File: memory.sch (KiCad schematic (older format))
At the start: 6 parts

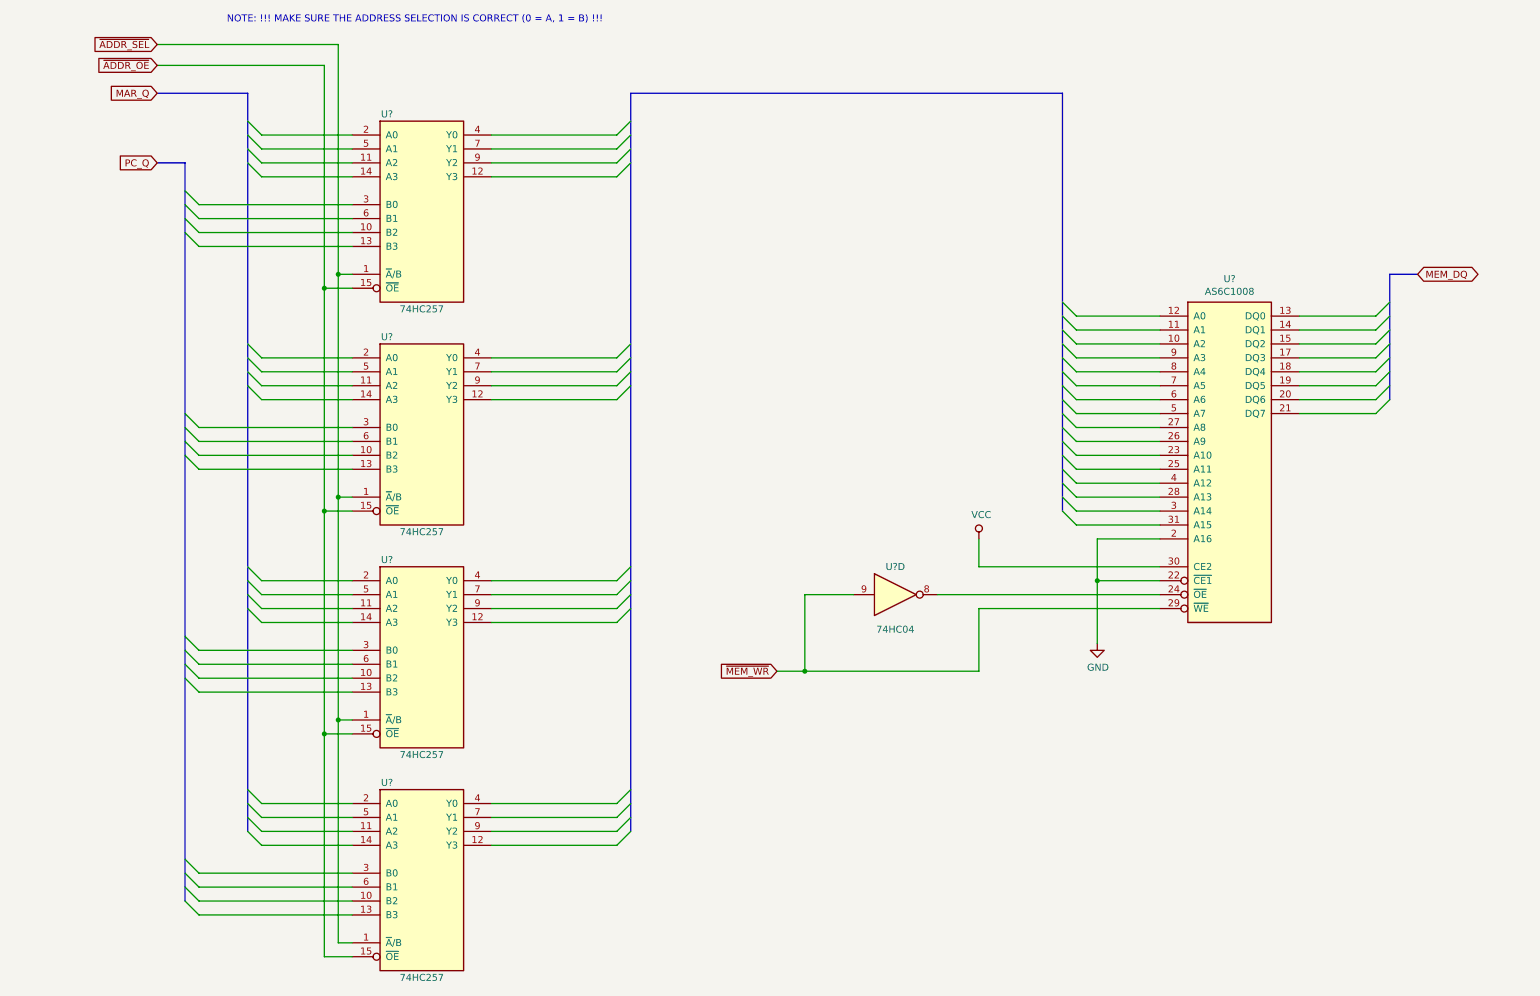
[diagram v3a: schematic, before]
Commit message: added labels
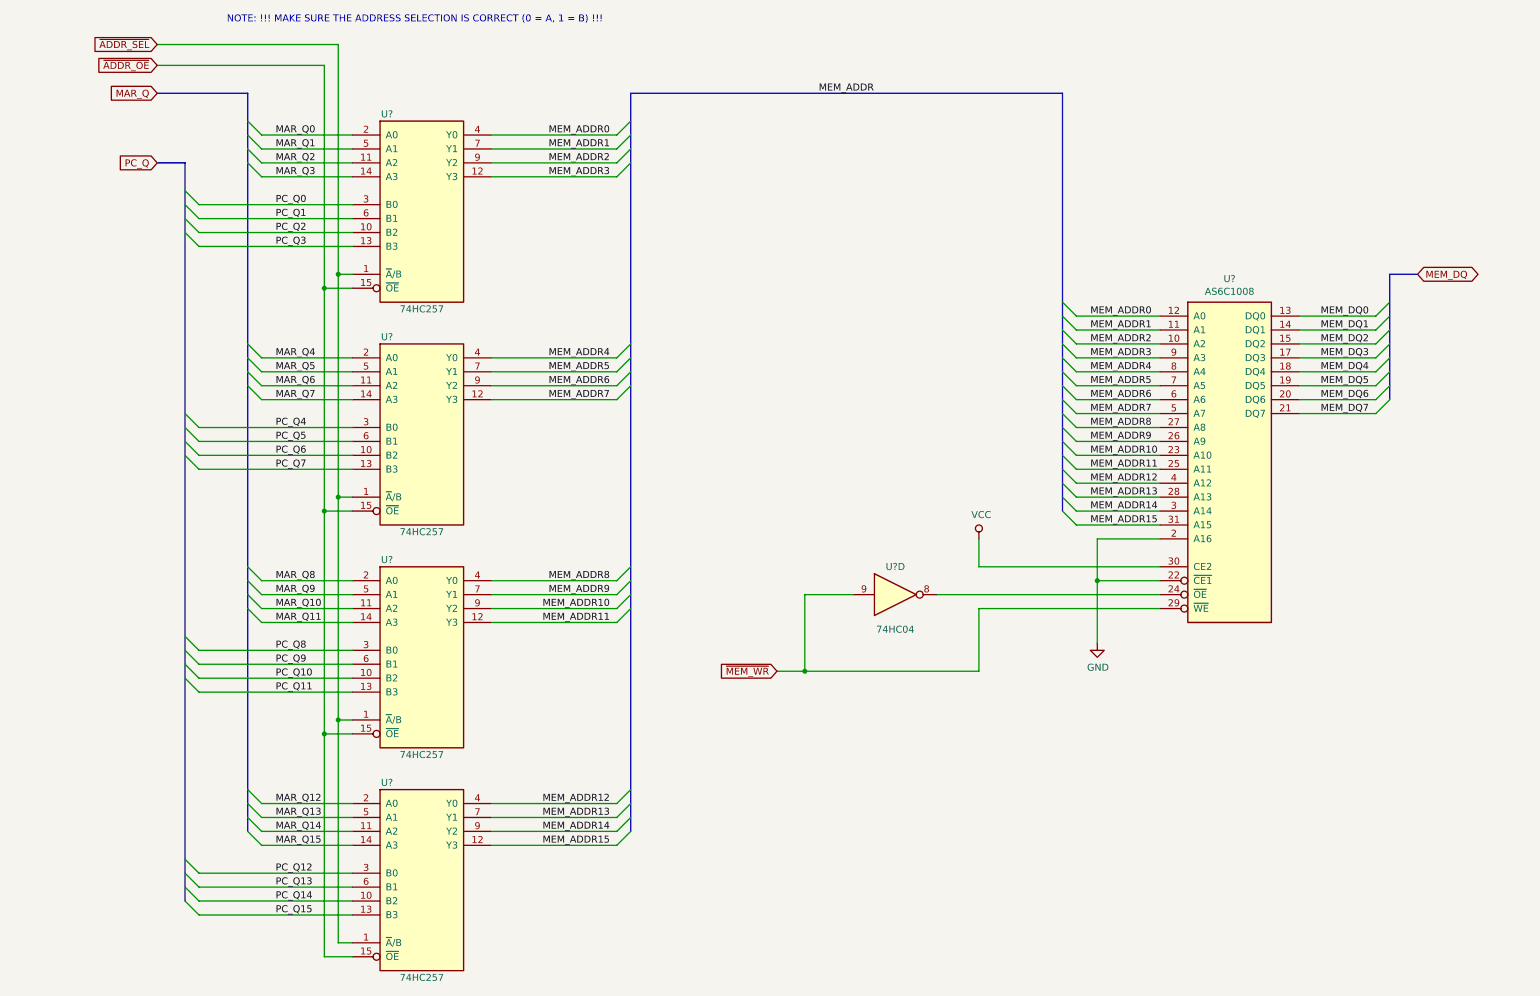
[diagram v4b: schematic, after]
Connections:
- net PC_Q2: now reaches U?.10 (B2)
- net MAR_Q2: now reaches U?.11 (A2)
- net MEM_ADDR3: now reaches U?.12 (Y3)
- net MEM_ADDR3: now also U?.9 (A3)
- net PC_Q3: now reaches U?.13 (B3)
- net MAR_Q3: now reaches U?.14 (A3)
- net MAR_Q0: now reaches U?.2 (A0)
- net PC_Q0: now reaches U?.3 (B0)
- net MEM_ADDR0: now reaches U?.4 (Y0)
- net MEM_ADDR0: now also U?.12 (A0)
- net MAR_Q1: now reaches U?.5 (A1)
- net PC_Q1: now reaches U?.6 (B1)
- net MEM_ADDR1: now reaches U?.7 (Y1)
- net MEM_ADDR1: now also U?.11 (A1)
- net MEM_ADDR2: now reaches U?.9 (Y2)
- net MEM_ADDR2: now also U?.10 (A2)
- net PC_Q6: now reaches U?.10 (B2)
- net MAR_Q6: now reaches U?.11 (A2)
- net MEM_ADDR7: now reaches U?.12 (Y3)
- net MEM_ADDR7: now also U?.5 (A7)
- net PC_Q7: now reaches U?.13 (B3)
- net MAR_Q7: now reaches U?.14 (A3)
- net MAR_Q4: now reaches U?.2 (A0)
- net PC_Q4: now reaches U?.3 (B0)
- net MEM_ADDR4: now reaches U?.4 (Y0)
- net MEM_ADDR4: now also U?.8 (A4)
- net MAR_Q5: now reaches U?.5 (A1)
- net PC_Q5: now reaches U?.6 (B1)
- net MEM_ADDR5: now reaches U?.7 (Y1)
- net MEM_ADDR5: now also U?.7 (A5)
- net MEM_ADDR6: now reaches U?.9 (Y2)
- net MEM_ADDR6: now also U?.6 (A6)
- net PC_Q10: now reaches U?.10 (B2)
- net MAR_Q10: now reaches U?.11 (A2)
- net MEM_ADDR11: now reaches U?.12 (Y3)
- net MEM_ADDR11: now also U?.25 (A11)
- net PC_Q11: now reaches U?.13 (B3)
- net MAR_Q11: now reaches U?.14 (A3)
- net MAR_Q8: now reaches U?.2 (A0)
- net PC_Q8: now reaches U?.3 (B0)
- net MEM_ADDR8: now reaches U?.4 (Y0)
- net MEM_ADDR8: now also U?.27 (A8)
- net MAR_Q9: now reaches U?.5 (A1)
- net PC_Q9: now reaches U?.6 (B1)
- net MEM_ADDR9: now reaches U?.7 (Y1)
- net MEM_ADDR9: now also U?.26 (A9)
- net MEM_ADDR10: now reaches U?.9 (Y2)
- net MEM_ADDR10: now also U?.23 (A10)
- net PC_Q14: now reaches U?.10 (B2)
- net MAR_Q14: now reaches U?.11 (A2)
- net MEM_ADDR15: now reaches U?.12 (Y3)
- net MEM_ADDR15: now also U?.31 (A15)
- net PC_Q15: now reaches U?.13 (B3)
- net MAR_Q15: now reaches U?.14 (A3)
- net MAR_Q12: now reaches U?.2 (A0)
- net PC_Q12: now reaches U?.3 (B0)
- net MEM_ADDR12: now reaches U?.4 (Y0)
- net MEM_ADDR12: now also U?.4 (A12)
- net MAR_Q13: now reaches U?.5 (A1)
- net PC_Q13: now reaches U?.6 (B1)
- net MEM_ADDR13: now reaches U?.7 (Y1)
- net MEM_ADDR13: now also U?.28 (A13)
- net MEM_ADDR14: now reaches U?.9 (Y2)
- net MEM_ADDR14: now also U?.3 (A14)
- net MEM_DQ0: now reaches U?.13 (DQ0)
- net MEM_DQ1: now reaches U?.14 (DQ1)
- net MEM_DQ2: now reaches U?.15 (DQ2)
- net MEM_DQ3: now reaches U?.17 (DQ3)
- net MEM_DQ4: now reaches U?.18 (DQ4)
- net MEM_DQ5: now reaches U?.19 (DQ5)
- net MEM_DQ6: now reaches U?.20 (DQ6)
- net MEM_DQ7: now reaches U?.21 (DQ7)
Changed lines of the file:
@@
 Wire Bus Line
 	1650 1750 1650 7050
+Text Label 2300 1550 0    50   ~ 0
+MAR_Q0
+Text Label 2300 1650 0    50   ~ 0
+MAR_Q1
+Text Label 2300 1750 0    50   ~ 0
+MAR_Q2
+Text Label 2300 1850 0    50   ~ 0
+MAR_Q3
+Text Label 2300 2050 0    50   ~ 0
+PC_Q0
+Text Label 2300 2150 0    50   ~ 0
+PC_Q1
+Text Label 2300 2250 0    50   ~ 0
+PC_Q2
+Text Label 2300 2350 0    50   ~ 0
+PC_Q3
+Text Label 2300 3150 0    50   ~ 0
+MAR_Q4
+Text Label 2300 3250 0    50   ~ 0
+MAR_Q5
+Text Label 2300 3350 0    50   ~ 0
+MAR_Q6
+Text Label 2300 3450 0    50   ~ 0
+MAR_Q7
+Text Label 2300 3650 0    50   ~ 0
+PC_Q4
+Text Label 2300 3750 0    50   ~ 0
+PC_Q5
+Text Label 2300 3850 0    50   ~ 0
+PC_Q6
+Text Label 2300 3950 0    50   ~ 0
+PC_Q7
+Text Label 2300 4750 0    50   ~ 0
+MAR_Q8
+Text Label 2300 4850 0    50   ~ 0
+MAR_Q9
+Text Label 2300 4950 0    50   ~ 0
+MAR_Q10
+Text Label 2300 5050 0    50   ~ 0
+MAR_Q11
+Text Label 2300 5250 0    50   ~ 0
+PC_Q8
+Text Label 2300 5350 0    50   ~ 0
+PC_Q9
+Text Label 2300 5450 0    50   ~ 0
+PC_Q10
+Text Label 2300 5550 0    50   ~ 0
+PC_Q11
+Text Label 2300 6350 0    50   ~ 0
+MAR_Q12
+Text Label 2300 6450 0    50   ~ 0
+MAR_Q13
+Text Label 2300 6550 0    50   ~ 0
+MAR_Q14
+Text Label 2300 6650 0    50   ~ 0
+MAR_Q15
+Text Label 2300 6850 0    50   ~ 0
+PC_Q12
+Text Label 2300 6950 0    50   ~ 0
+PC_Q13
+Text Label 2300 7050 0    50   ~ 0
+PC_Q14
+Text Label 2300 7150 0    50   ~ 0
+PC_Q15
+Text Label 4700 1550 2    50   ~ 0
+MEM_ADDR0
+Text Label 4700 1650 2    50   ~ 0
+MEM_ADDR1
+Text Label 4700 1750 2    50   ~ 0
+MEM_ADDR2
+Text Label 4700 1850 2    50   ~ 0
+MEM_ADDR3
+Text Label 4700 3150 2    50   ~ 0
+MEM_ADDR4
+Text Label 4700 3250 2    50   ~ 0
+MEM_ADDR5
+Text Label 4700 3350 2    50   ~ 0
+MEM_ADDR6
+Text Label 4700 3450 2    50   ~ 0
+MEM_ADDR7
+Text Label 4700 4750 2    50   ~ 0
+MEM_ADDR8
+Text Label 4700 4850 2    50   ~ 0
+MEM_ADDR9
+Text Label 4700 4950 2    50   ~ 0
+MEM_ADDR10
+Text Label 4700 5050 2    50   ~ 0
+MEM_ADDR11
+Text Label 4700 6350 2    50   ~ 0
+MEM_ADDR12
+Text Label 4700 6450 2    50   ~ 0
+MEM_ADDR13
+Text Label 4700 6550 2    50   ~ 0
+MEM_ADDR14
+Text Label 4700 6650 2    50   ~ 0
+MEM_ADDR15
+Text Label 8150 2850 0    50   ~ 0
+MEM_ADDR0
+Text Label 8150 2950 0    50   ~ 0
+MEM_ADDR1
+Text Label 8150 3050 0    50   ~ 0
+MEM_ADDR2
+Text Label 8150 3150 0    50   ~ 0
+MEM_ADDR3
+Text Label 8150 3250 0    50   ~ 0
+MEM_ADDR4
+Text Label 8150 3350 0    50   ~ 0
+MEM_ADDR5
+Text Label 8150 3450 0    50   ~ 0
+MEM_ADDR6
+Text Label 8150 3550 0    50   ~ 0
+MEM_ADDR7
+Text Label 8150 3650 0    50   ~ 0
+MEM_ADDR8
+Text Label 8150 3750 0    50   ~ 0
+MEM_ADDR9
+Text Label 8150 3850 0    50   ~ 0
+MEM_ADDR10
+Text Label 8150 3950 0    50   ~ 0
+MEM_ADDR11
+Text Label 8150 4050 0    50   ~ 0
+MEM_ADDR12
+Text Label 8150 4150 0    50   ~ 0
+MEM_ADDR13
+Text Label 8150 4250 0    50   ~ 0
+MEM_ADDR14
+Text Label 8150 4350 0    50   ~ 0
+MEM_ADDR15
+Text Label 6200 1250 0    50   ~ 0
+MEM_ADDR
+Text Label 10150 2850 2    50   ~ 0
+MEM_DQ0
+Text Label 10150 2950 2    50   ~ 0
+MEM_DQ1
+Text Label 10150 3050 2    50   ~ 0
+MEM_DQ2
+Text Label 10150 3150 2    50   ~ 0
+MEM_DQ3
+Text Label 10150 3250 2    50   ~ 0
+MEM_DQ4
+Text Label 10150 3350 2    50   ~ 0
+MEM_DQ5
+Text Label 10150 3450 2    50   ~ 0
+MEM_DQ6
+Text Label 10150 3550 2    50   ~ 0
+MEM_DQ7
 $EndSCHEMATC

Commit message: done for the night passing drc
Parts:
- gave numbers to parts that had none: 6
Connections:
- net ~ADDR_SEL renamed ~SEL_ADDR_PC_MAR
- net ~MEM_WR renamed ~WR_MEM
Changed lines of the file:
@@
 $Descr A4 11693 8268
 encoding utf-8
-Sheet 4 6
+Sheet 4 7
 Title ""
 Date ""
@@
 $EndDescr
 $Comp
-L 74xx_modified:AS6C1008 U?
+L 74xx_modified:AS6C1008 U17
 U 1 1 5CBBFD35
 P 9150 3400
-F 0 "U?" H 9150 4217 50  0000 C CNN
+F 0 "U17" H 9150 4217 50  0000 C CNN
 F 1 "AS6C1008" H 9150 4126 50  0000 C CNN
 F 2 "" H 9100 3400 50  0001 C CNN
@@
 	10300 2550 10500 2550
 Text GLabel 10500 2550 2    50   BiDi ~ 0
-MEM_DQ
+MEM_DQ[0..15]
 Entry Wire Line
 	7950 4250 8050 4350
@@
 	7350 4650 7350 4450
 $Comp
-L power:VCC #PWR?
+L power:VCC #PWR04
 U 1 1 5CBC2B7B
 P 7350 4450
-F 0 "#PWR?" H 7350 4300 50  0001 C CNN
+F 0 "#PWR04" H 7350 4300 50  0001 C CNN
 F 1 "VCC" H 7367 4623 50  0000 C CNN
 F 2 "" H 7350 4450 50  0001 C CNN
@@
 $EndComp
 $Comp
-L 74xx_modified:74LS257 U?
+L 74xx_modified:74LS257 U13
 U 1 1 5C55466F
 P 3350 2150
-F 0 "U?" H 3100 2900 50  0000 C CNN
+F 0 "U13" H 3100 2900 50  0000 C CNN
 F 1 "74HC257" H 3350 1500 50  0000 C CNN
 F 2 "" H 3350 2150 50  0001 C CNN
@@
 $EndComp
 $Comp
-L 74xx_modified:74LS257 U?
+L 74xx_modified:74LS257 U14
 U 1 1 5C5601F9
 P 3350 3750
-F 0 "U?" H 3100 4500 50  0000 C CNN
+F 0 "U14" H 3100 4500 50  0000 C CNN
 F 1 "74HC257" H 3350 3100 50  0000 C CNN
 F 2 "" H 3350 3750 50  0001 C CNN
@@
 $EndComp
 $Comp
-L 74xx_modified:74LS257 U?
+L 74xx_modified:74LS257 U16
 U 1 1 5C560317
 P 3350 6950
-F 0 "U?" H 3100 7700 50  0000 C CNN
+F 0 "U16" H 3100 7700 50  0000 C CNN
 F 1 "74HC257" H 3350 6300 50  0000 C CNN
 F 2 "" H 3350 6950 50  0001 C CNN
@@
 	2850 4750 2200 4750
 $Comp
-L 74xx_modified:74LS257 U?
+L 74xx_modified:74LS257 U15
 U 1 1 5C5602CB
 P 3350 5350
-F 0 "U?" H 3100 6100 50  0000 C CNN
+F 0 "U15" H 3100 6100 50  0000 C CNN
 F 1 "74HC257" H 3350 4700 50  0000 C CNN
 F 2 "" H 3350 5350 50  0001 C CNN
@@
 	1450 1250 2100 1250
 Text GLabel 1450 900  0    50   Input ~ 0
-~ADDR_SEL
+~SEL_ADDR_PC_MAR
 Text GLabel 1450 1050 0    50   Input ~ 0
 ~ADDR_OE
 Text GLabel 1450 1250 0    50   Input ~ 0
-MAR_Q
+MAR_Q[0..15]
 Text GLabel 1450 1750 0    50   Input ~ 0
-PC_Q
+PC_Q[0..15]
 Text Notes 1950 750  0    50   ~ 0
 NOTE: !!! MAKE SURE THE ADDRESS SELECTION IS CORRECT (0 = A, 1 = B) !!!
 Text GLabel 5900 5400 0    50   Input ~ 0
-~MEM_WR
+~WR_MEM
 $Comp
 L 74xx:74LS04 U?
@@
 AR Path="/5CB820A3/5C5FDD6B" Ref="U?"  Part="3"
 AR Path="/5C4D52FD/5C5FDD6B" Ref="U?"  Part="3"
-AR Path="/5CBABD04/5C5FDD6B" Ref="U?"  Part="4"
-F 0 "U?" H 6750 5050 50  0000 C CNN
+AR Path="/5CBABD04/5C5FDD6B" Ref="U8"  Part="4"
+F 0 "U8" H 6750 5050 50  0000 C CNN
 F 1 "74HC04" H 6750 4600 50  0000 C CNN
 F 2 "Package_DIP:DIP-14_W7.62mm" H 6750 4850 50  0001 C CNN
@@
 	8200 4750 8200 5200
 $Comp
-L power:GND #PWR?
+L power:GND #PWR05
 U 1 1 5C637105
 P 8200 5200
-F 0 "#PWR?" H 8200 4950 50  0001 C CNN
+F 0 "#PWR05" H 8200 4950 50  0001 C CNN
 F 1 "GND" H 8205 5027 50  0000 C CNN
 F 2 "" H 8200 5200 50  0001 C CNN
@@
 MEM_ADDR15
 Text Label 6200 1250 0    50   ~ 0
-MEM_ADDR
+MEM_ADDR[0..15]
 Text Label 10150 2850 2    50   ~ 0
 MEM_DQ0

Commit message: calling it a night
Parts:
- U13, U14, U15, U16: footprint (none) -> Package_DIP:DIP-16_W7.62mm
- U17: footprint (none) -> Package_DIP:DIP-32_W15.24mm
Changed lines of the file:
@@
 F 0 "U17" H 9150 4217 50  0000 C CNN
 F 1 "AS6C1008" H 9150 4126 50  0000 C CNN
-F 2 "" H 9100 3400 50  0001 C CNN
+F 2 "Package_DIP:DIP-32_W15.24mm" H 9100 3400 50  0001 C CNN
 F 3 "" H 9100 3400 50  0001 C CNN
 	1    9150 3400
@@
 F 0 "U13" H 3100 2900 50  0000 C CNN
 F 1 "74HC257" H 3350 1500 50  0000 C CNN
-F 2 "" H 3350 2150 50  0001 C CNN
+F 2 "Package_DIP:DIP-16_W7.62mm" H 3350 2150 50  0001 C CNN
 F 3 "http://www.ti.com/lit/gpn/sn74LS257" H 3350 2150 50  0001 C CNN
 	1    3350 2150
@@
 F 0 "U14" H 3100 4500 50  0000 C CNN
 F 1 "74HC257" H 3350 3100 50  0000 C CNN
-F 2 "" H 3350 3750 50  0001 C CNN
+F 2 "Package_DIP:DIP-16_W7.62mm" H 3350 3750 50  0001 C CNN
 F 3 "http://www.ti.com/lit/gpn/sn74LS257" H 3350 3750 50  0001 C CNN
 	1    3350 3750
@@
 F 0 "U16" H 3100 7700 50  0000 C CNN
 F 1 "74HC257" H 3350 6300 50  0000 C CNN
-F 2 "" H 3350 6950 50  0001 C CNN
+F 2 "Package_DIP:DIP-16_W7.62mm" H 3350 6950 50  0001 C CNN
 F 3 "http://www.ti.com/lit/gpn/sn74LS257" H 3350 6950 50  0001 C CNN
 	1    3350 6950
@@
 F 0 "U15" H 3100 6100 50  0000 C CNN
 F 1 "74HC257" H 3350 4700 50  0000 C CNN
-F 2 "" H 3350 5350 50  0001 C CNN
+F 2 "Package_DIP:DIP-16_W7.62mm" H 3350 5350 50  0001 C CNN
 F 3 "http://www.ti.com/lit/gpn/sn74LS257" H 3350 5350 50  0001 C CNN
 	1    3350 5350
